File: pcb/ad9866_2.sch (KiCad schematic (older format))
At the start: 103 parts, among them CN1 MEC6-140_CONNECTOR_BEMICRO, CON1 USB-MICRO-B, P1 CONN_2, P10 CONN_1, P2 CONN_10X2, P3 CONN_1, P4 CONN_5X2, P5 CONN_1, P5V0 CONN_1, P6 Coaxial_Connector, P7 Coaxial_Connector, P8 CONN_2, P9 CONN_1, Q1 Si2301, T1 TRANSF_ADT2, T2 TRANSF_ADT8, U1 NCP1117ST33T3G, U2 NCP1117ST33T3G, U3 Si510, U4 AD9866BCPZ, U5 NCP1117ST33T3G, U6 25AA02E48T-I/OT

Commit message: Revised after first review.
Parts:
- removed P5, PGND1: CONN_1, symbol CONN_1
- added C11, C13: 0.1UF, symbol Csmall
- added FB35: FB, symbol FB
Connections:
- net GND: now also T2.1 (S2), C11.1, C13.1; no longer T2.3 (S1)
- net VIN: now also C13.2, FB35.1; no longer CN1.79 (5V), CN1.80 (5V)
- net at C32.1: now also T2.3 (S1); no longer T2.1 (S2)
- net at T2.4 (PR2): now also C18.1; no longer C19.1
- net at T2.6 (PR1): now also C19.1; no longer C18.1
- new net: C11.2, CN1.79 (5V), CN1.80 (5V), FB35.2
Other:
- moved on the sheet: P5V0

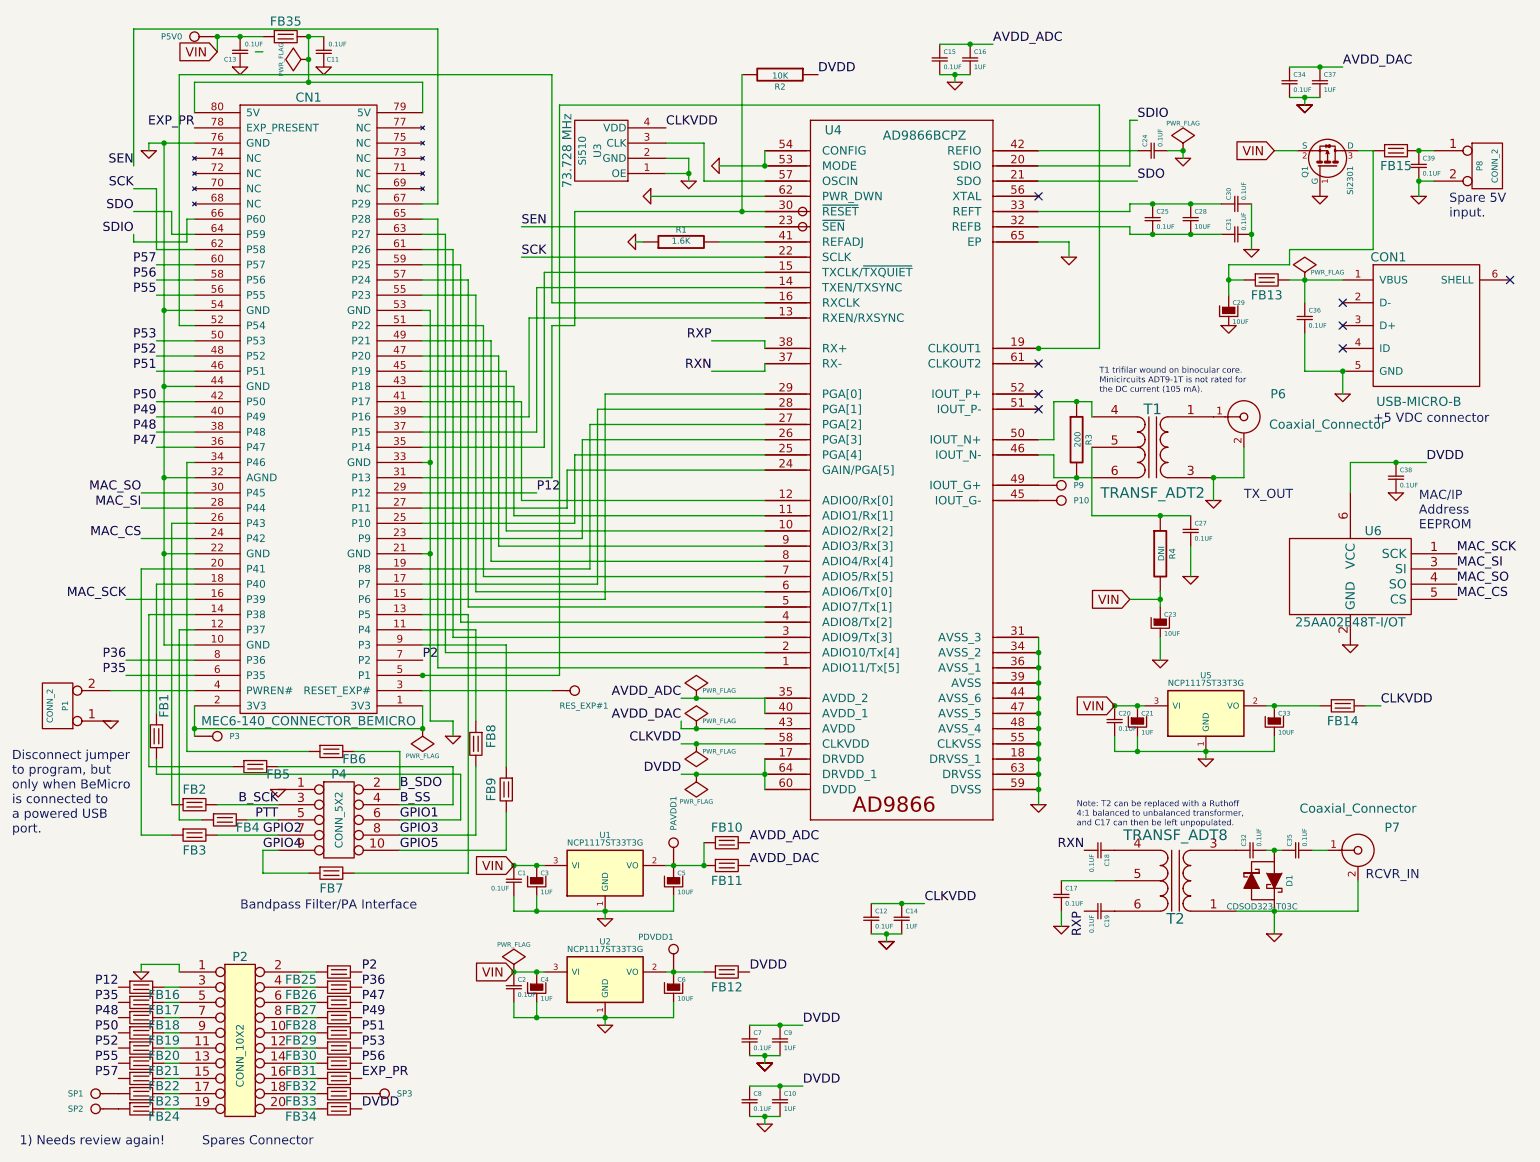
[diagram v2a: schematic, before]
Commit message: Added more FB's and bypass caps.
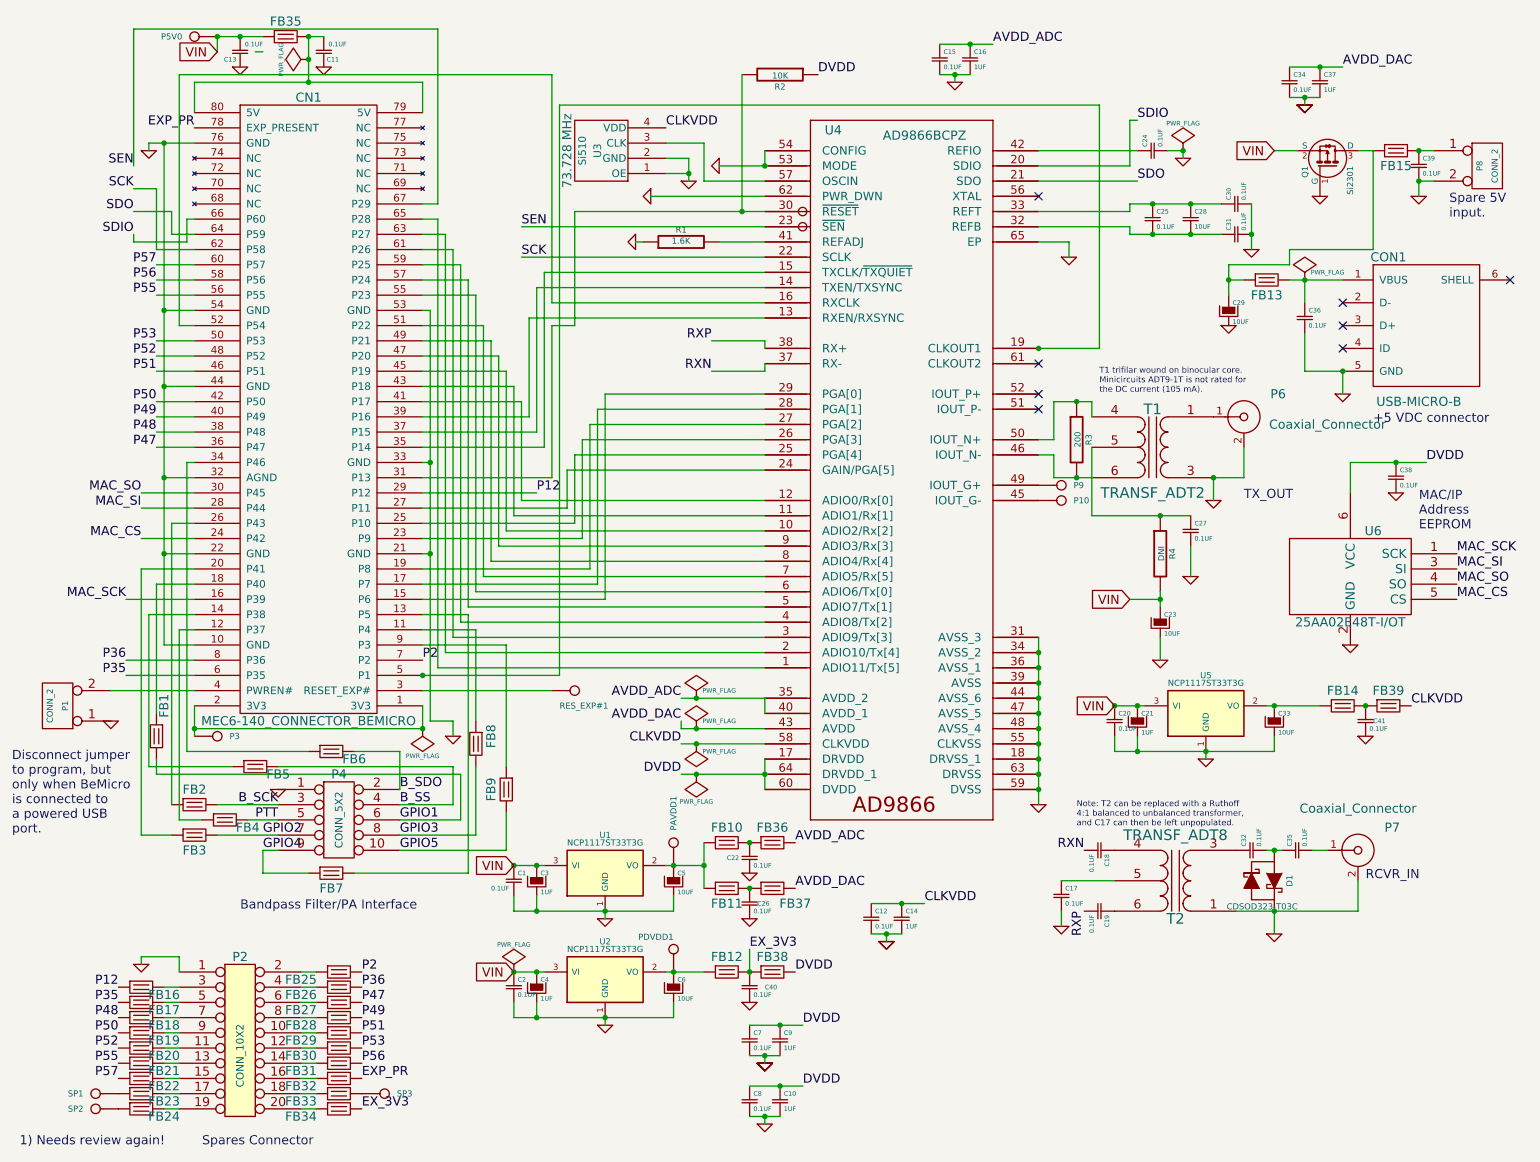
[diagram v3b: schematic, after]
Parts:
- added C22, C26, C40, C41: 0.1UF, symbol Csmall
- added FB36, FB37, FB38, FB39: FB, symbol FB
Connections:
- net AVDD_ADC: now also FB36.2; no longer FB10.2
- net AVDD_DAC: now also FB37.2; no longer FB11.2
- net CLKVDD: now also FB39.2; no longer FB14.2
- net DVDD: now also FB38.2; no longer FB12.2, FB34.2
- net GND: now also C22.2, C26.2, C40.2, C41.2
- new net: C26.1, FB11.2, FB37.1
- new net: C22.1, FB10.2, FB36.1
- new net: C41.1, FB14.2, FB39.1
- new net EX_3V3: C40.1, FB12.2, FB34.2, FB38.1
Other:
- moved on the sheet: FB11
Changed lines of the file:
@@
 Text Notes 600  7900 0    60   ~ 0
 1) Needs review again!\n
-Text Label 9550 5000 0    60   ~ 0
+Text Label 9750 5000 0    60   ~ 0
 CLKVDD
 Text Label 6550 6300 0    60   ~ 0
@@
 Text Label 4950 4950 2    60   ~ 0
 AVDD_ADC
-Text Label 5400 5900 0    60   ~ 0
+Text Label 5700 5900 0    60   ~ 0
 AVDD_ADC
-Text Label 5400 6050 0    60   ~ 0
+Text Label 5700 6200 0    60   ~ 0
 AVDD_DAC
 Text Label 9850 3400 0    60   ~ 0
@@
 Text Label 5150 2800 2    60   ~ 0
 RXN
-Text Label 5400 6750 0    60   ~ 0
+Text Label 5700 6750 0    60   ~ 0
 DVDD
 Text Label 5750 7100 0    60   ~ 0
@@
 U 1 1 5371AC94
 P 5250 6750
-F 0 "FB12" H 5250 6650 60  0000 C CNN
+F 0 "FB12" H 5250 6850 60  0000 C CNN
 F 1 "FB" H 5250 6850 60  0001 C CNN
 F 2 "" H 5250 6750 60  0000 C CNN
@@
 L FB FB11
 U 1 1 5371ACA8
-P 5250 6050
-F 0 "FB11" H 5250 5950 60  0000 C CNN
-F 1 "FB" H 5250 6150 60  0001 C CNN
-F 2 "" H 5250 6050 60  0000 C CNN
-F 3 "" H 5250 6050 60  0000 C CNN
-	1    5250 6050
+P 5250 6200
+F 0 "FB11" H 5250 6100 60  0000 C CNN
+F 1 "FB" H 5250 6300 60  0001 C CNN
+F 2 "" H 5250 6200 60  0000 C CNN
+F 3 "" H 5250 6200 60  0000 C CNN
+	1    5250 6200
 	1    0    0    -1
 $EndComp
@@
 U 1 1 5371CBCD
 P 9300 5000
-F 0 "FB14" H 9300 4900 60  0000 C CNN
+F 0 "FB14" H 9300 5100 60  0000 C CNN
 F 1 "FB" H 9300 5100 60  0001 C CNN
 F 2 "" H 9300 5000 60  0000 C CNN
@@
 L GND #PWR044
 U 1 1 53988412
-P 1400 6750
-F 0 "#PWR044" H 1400 6750 30  0001 C CNN
-F 1 "GND" H 1400 6680 30  0001 C CNN
-F 2 "" H 1400 6750 60  0000 C CNN
-F 3 "" H 1400 6750 60  0000 C CNN
-	1    1400 6750
-	1    0    0    -1
-$EndComp
-Text Label 2850 7650 0    60   ~ 0
-DVDD
+P 1400 6700
+F 0 "#PWR044" H 1400 6700 30  0001 C CNN
+F 1 "GND" H 1400 6630 30  0001 C CNN
+F 2 "" H 1400 6700 60  0000 C CNN
+F 3 "" H 1400 6700 60  0000 C CNN
+	1    1400 6700
+	1    0    0    -1
+$EndComp
 Text Notes 1800 7900 0    60   ~ 0
 Spares Connector\n
@@
 	1500 4200 1500 5050
 Wire Wire Line
-	5100 6050 5100 5900
+	5100 5900 5100 6200
 Wire Wire Line
 	1650 5750 1800 5750
 Wire Wire Line
 	8550 2200 8650 2200
-Wire Wire Line
-	9450 5000 9550 5000
 Wire Wire Line
 	3250 3600 4000 3600
@@
 	1550 7450 1650 7450
 Wire Wire Line
-	1650 6750 1650 6700
-Wire Wire Line
-	1650 6700 1400 6700
-Wire Wire Line
-	1400 6700 1400 6750
+	1650 6750 1650 6650
+Wire Wire Line
+	1650 6650 1400 6650
+Wire Wire Line
+	1400 6650 1400 6700
 Wire Wire Line
 	1550 7550 1650 7550
@@
 Wire Wire Line
 	2500 600  2600 600
+$Comp
+L Csmall C22
+U 1 1 53A4595F
+P 5400 6000
+F 0 "C22" H 5250 6000 30  0000 L CNN
+F 1 "0.1UF" H 5425 5950 30  0000 L CNN
+F 2 "" H 5400 6000 60  0000 C CNN
+F 3 "" H 5400 6000 60  0000 C CNN
+	1    5400 6000
+	1    0    0    -1
+$EndComp
+$Comp
+L Csmall C26
+U 1 1 53A45C9A
+P 5400 6300
+F 0 "C26" H 5450 6300 30  0000 L CNN
+F 1 "0.1UF" H 5425 6250 30  0000 L CNN
+F 2 "" H 5400 6300 60  0000 C CNN
+F 3 "" H 5400 6300 60  0000 C CNN
+	1    5400 6300
+	1    0    0    -1
+$EndComp
+$Comp
+L FB FB36
+U 1 1 53A45E06
+P 5550 5900
+F 0 "FB36" H 5550 6000 60  0000 C CNN
+F 1 "FB" H 5550 6000 60  0001 C CNN
+F 2 "" H 5550 5900 60  0000 C CNN
+F 3 "" H 5550 5900 60  0000 C CNN
+	1    5550 5900
+	1    0    0    -1
+$EndComp
+$Comp
+L FB FB37
+U 1 1 53A45E95
+P 5550 6200
+F 0 "FB37" H 5700 6100 60  0000 C CNN
+F 1 "FB" H 5550 6300 60  0001 C CNN
+F 2 "" H 5550 6200 60  0000 C CNN
+F 3 "" H 5550 6200 60  0000 C CNN
+	1    5550 6200
+	1    0    0    -1
+$EndComp
+$Comp
+L GND #PWR048
+U 1 1 53A461CF
+P 5400 6400
+F 0 "#PWR048" H 5400 6400 30  0001 C CNN
+F 1 "GND" H 5400 6330 30  0001 C CNN
+F 2 "" H 5400 6400 60  0000 C CNN
+F 3 "" H 5400 6400 60  0000 C CNN
+	1    5400 6400
+	1    0    0    -1
+$EndComp
+$Comp
+L GND #PWR049
+U 1 1 53A46246
+P 5400 6100
+F 0 "#PWR049" H 5400 6100 30  0001 C CNN
+F 1 "GND" H 5400 6030 30  0001 C CNN
+F 2 "" H 5400 6100 60  0000 C CNN
+F 3 "" H 5400 6100 60  0000 C CNN
+	1    5400 6100
+	1    0    0    -1
+$EndComp
+$Comp
+L FB FB38
+U 1 1 53A466FB
+P 5550 6750
+F 0 "FB38" H 5550 6850 60  0000 C CNN
+F 1 "FB" H 5550 6850 60  0001 C CNN
+F 2 "" H 5550 6750 60  0000 C CNN
+F 3 "" H 5550 6750 60  0000 C CNN
+	1    5550 6750
+	1    0    0    -1
+$EndComp
+$Comp
+L Csmall C40
+U 1 1 53A46796
+P 5400 6850
+F 0 "C40" H 5500 6850 30  0000 L CNN
+F 1 "0.1UF" H 5425 6800 30  0000 L CNN
+F 2 "" H 5400 6850 60  0000 C CNN
+F 3 "" H 5400 6850 60  0000 C CNN
+	1    5400 6850
+	1    0    0    -1
+$EndComp
+$Comp
+L GND #PWR050
+U 1 1 53A46BC0
+P 5400 6950
+F 0 "#PWR050" H 5400 6950 30  0001 C CNN
+F 1 "GND" H 5400 6880 30  0001 C CNN
+F 2 "" H 5400 6950 60  0000 C CNN
+F 3 "" H 5400 6950 60  0000 C CNN
+	1    5400 6950
+	1    0    0    -1
+$EndComp
+$Comp
+L Csmall C41
+U 1 1 53A47C29
+P 9450 5100
+F 0 "C41" H 9500 5100 30  0000 L CNN
+F 1 "0.1UF" H 9475 5050 30  0000 L CNN
+F 2 "" H 9450 5100 60  0000 C CNN
+F 3 "" H 9450 5100 60  0000 C CNN
+	1    9450 5100
+	1    0    0    -1
+$EndComp
+$Comp
+L GND #PWR051
+U 1 1 53A47D0E
+P 9450 5200
+F 0 "#PWR051" H 9450 5200 30  0001 C CNN
+F 1 "GND" H 9450 5130 30  0001 C CNN
+F 2 "" H 9450 5200 60  0000 C CNN
+F 3 "" H 9450 5200 60  0000 C CNN
+	1    9450 5200
+	1    0    0    -1
+$EndComp
+$Comp
+L FB FB39
+U 1 1 53A47D88
+P 9600 5000
+F 0 "FB39" H 9600 5100 60  0000 C CNN
+F 1 "FB" H 9600 5100 60  0001 C CNN
+F 2 "" H 9600 5000 60  0000 C CNN
+F 3 "" H 9600 5000 60  0000 C CNN
+	1    9600 5000
+	1    0    0    -1
+$EndComp
+Connection ~ 9450 5000
+Connection ~ 5400 5900
+Connection ~ 5400 6200
+Connection ~ 5400 6750
+Text Label 2850 7650 0    60   ~ 0
+EX_3V3
+Text Label 5400 6600 0    60   ~ 0
+EX_3V3
+Wire Wire Line
+	5400 6600 5400 6750
 $EndSCHEMATC

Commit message: Cosmetic fixes to schematic.
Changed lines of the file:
@@
 U 1 1 53A1352F
 P 2350 600
-F 0 "FB35" H 2350 700 60  0000 C CNN
+F 0 "FB35" V 2250 500 60  0000 C CNN
 F 1 "FB" H 2350 700 60  0001 C CNN
 F 2 "" H 2350 600 60  0000 C CNN
@@
 	1    0    0    -1
 $EndComp
-Wire Wire Line
-	2150 700  2200 700
 $Comp
 L Csmall C13
